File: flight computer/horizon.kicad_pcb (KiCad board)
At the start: 4 copper layers, 50.8 x 95.7 mm, 138 parts, among them J1 Micro_SD_Card_Det1, J10 Conn_01x02_Pin, J11 USB_C_Receptacle_USB2.0_16P, J12 Conn_01x04, J13 1x3 servo, J14 1x3 servo, J15 arming terminal, J16 arming terminal, J17 H9161TR-ND, J18 Conn_02x03_Counter_Clockwise, J19 Screw_Terminal_01x02, J20 Screw_Terminal_01x02, J21 Conn_02x03_Counter_Clockwise, J3 H9161TR-ND, J4 H9161TR-ND, J5 Screw_Term, J6 1x3 servo, J9 1x3 servo, Q2 DMG2301L, Q7 BSS138, Q8 IRLML6402, Q9 IRLML6402, SW1 CK_KMS2xxG, U1 MMCU, U13 LTC4412xS6, U15 AP2112K-3.3, U16 SX1262IMLTRT, U17 PE4259, U2 MKL02Z32VFG4, U3 TPS61200DRC, U6 GPS, U8 NAND, U9 TPS82130, Y1 Crystal, Y2 32MHz

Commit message: wiring we can finish in lit 1-2 days max
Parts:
- removed R14: 1.5k, Resistor_SMD:R_0603_1608Metric
- moved C46 162.5 mm to (215.5, 106.4), turned to -90 degrees
- moved J4 161.2 mm to (211.7, 100.8), turned to 180 degrees
- moved C49 160.2 mm to (213.2, 103.9), turned to 90 degrees
- moved R8 158.8 mm to (215.5, 103.3), turned to -90 degrees
- moved FL1 158.8 mm to (213.0, 110.0), turned to 90 degrees
- moved C48 154.3 mm to (210.6, 109.7), turned to 90 degrees
- moved U17 153.3 mm to (213.3, 107.0), turned to 90 degrees
- moved L10 152.7 mm to (211.3, 112.0)
- moved C47 151.9 mm to (209.0, 109.7), turned to 90 degrees
- moved C14 92.7 mm to (118.9, 142.7), turned to 45 degrees
- moved C37 90.0 mm to (124.9, 148.7)
- moved C40 89.9 mm to (123.5, 152.1)
- moved C38 89.6 mm to (121.5, 142.3), turned to 90 degrees
- moved C39 85.3 mm to (118.3, 148.5), turned to -45 degrees
- moved U16 84.6 mm to (124.9, 145.3)
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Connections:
- SAMD21G18A-AU1 pad 33: D+ DMCU-1 -> D- DMCU-1
- SAMD21G18A-AU1 pad 34: D- DMCU-1 -> D+ DMCU-1
- SAMD21G18A-AU2 pad 33: D+ DMCU-2 -> D- DMCU-1
- SAMD21G18A-AU2 pad 34: D- DMCU-2 -> D+ DMCU-1
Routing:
- net Earth: track 0.00 -> 14.4 mm
- net SX_XTB: track 0.00 -> 7.24 mm
- net SX_XTA: track 0.00 -> 6.27 mm
- net Net-(U16-VREG): track 0.00 -> 5.16 mm
- net +3V3: track 0.00 -> 5.07 mm
- net Net-(U16-DCC_SW): track 0.00 -> 3.23 mm

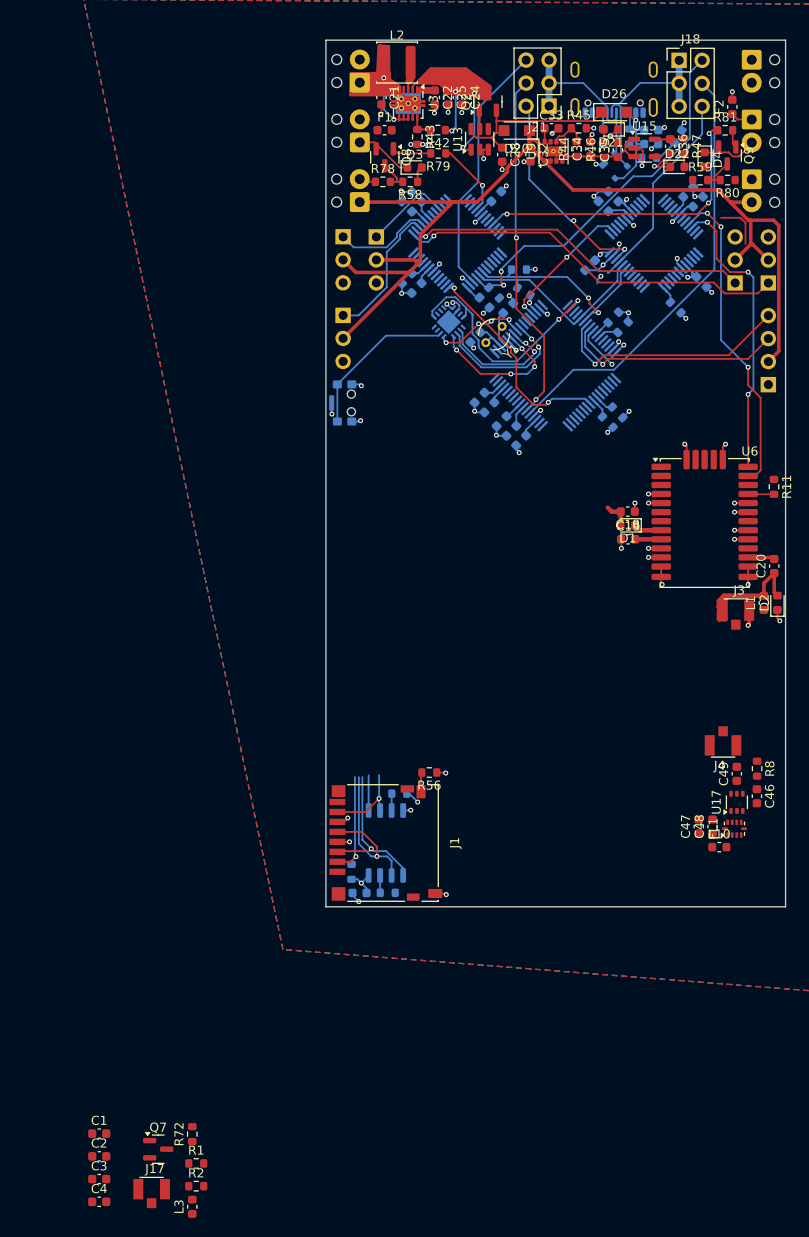
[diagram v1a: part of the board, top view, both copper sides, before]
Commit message: added BGM220SC12WGA2R
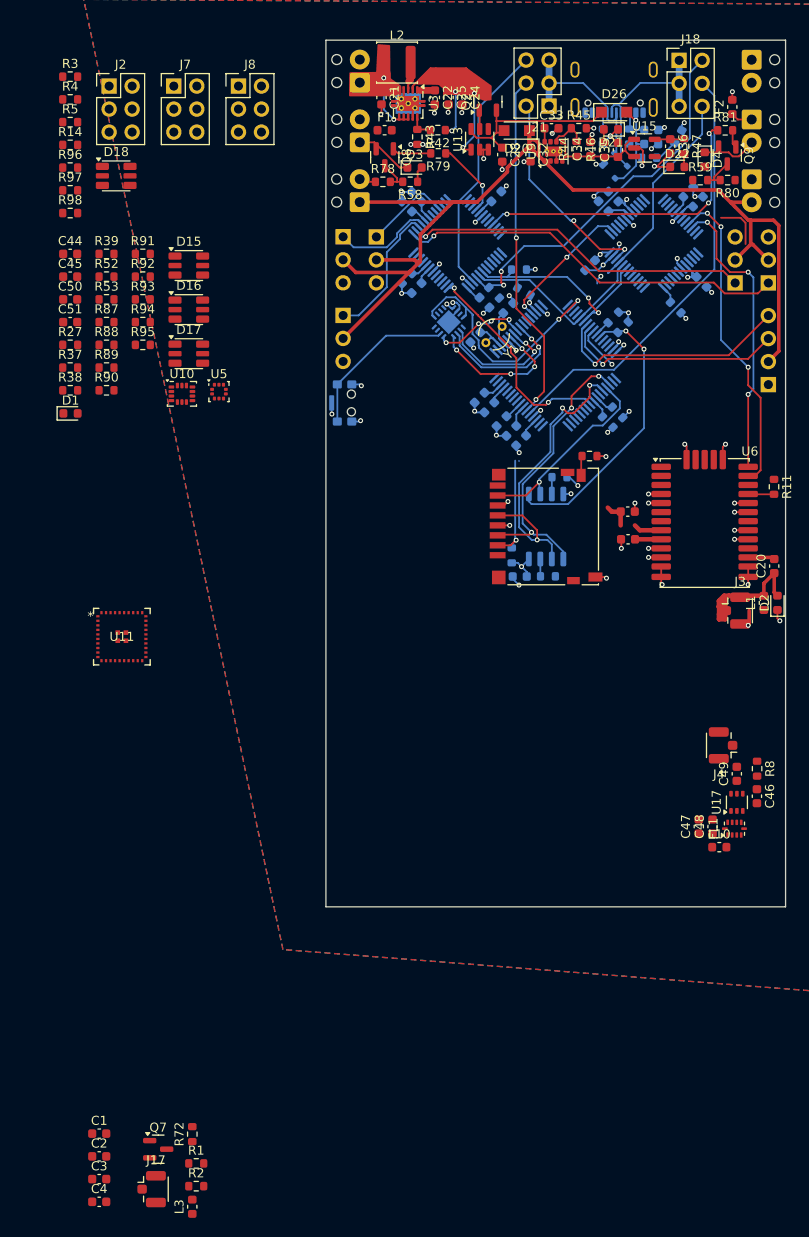
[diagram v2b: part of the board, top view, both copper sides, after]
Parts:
- added C44: 100nF, Capacitor_SMD:C_0603_1608Metric, F.Cu at (139.6, 46.5)
- added C45: 100nF, Capacitor_SMD:C_0603_1608Metric, F.Cu at (139.6, 49.0)
- added C50: 100nF, Capacitor_SMD:C_0603_1608Metric, F.Cu at (139.6, 51.5)
- added C51: 100nF, Capacitor_SMD:C_0603_1608Metric, F.Cu at (139.6, 54.0)
- added D15: SMLVN6RGB, LED_SMD:LED_ROHM_SMLVN6, F.Cu at (152.7, 47.8)
- added D16: SMLVN6RGB, LED_SMD:LED_ROHM_SMLVN6, F.Cu at (152.7, 52.6)
- added D17: SMLVN6RGB, LED_SMD:LED_ROHM_SMLVN6, F.Cu at (152.7, 57.5)
- added D18: SMLVN6RGB, LED_SMD:LED_ROHM_SMLVN6, F.Cu at (144.7, 37.9)
- added J2: Conn_02x03_Counter_Clockwise, Connector_PinHeader_2.54mm:PinHeader_2x03_P2.54mm_Vertical, F.Cu at (143.9, 28.0)
- added J7: Conn_02x03_Counter_Clockwise, Connector_PinHeader_2.54mm:PinHeader_2x03_P2.54mm_Vertical, F.Cu at (151.1, 28.0)
- added J8: Conn_02x03_Counter_Clockwise, Connector_PinHeader_2.54mm:PinHeader_2x03_P2.54mm_Vertical, F.Cu at (158.2, 28.0)
- added R14: 1.5k, Resistor_SMD:R_0603_1608Metric, F.Cu at (139.6, 34.5)
- added R27: 10k, Resistor_SMD:R_0603_1608Metric, F.Cu at (139.6, 56.5)
- added R3: 10k, Resistor_SMD:R_0603_1608Metric, F.Cu at (139.6, 26.9)
- added R37: 10k, Resistor_SMD:R_0603_1608Metric, F.Cu at (139.6, 59.0)
- added R38: 10k, Resistor_SMD:R_0603_1608Metric, F.Cu at (139.6, 61.5)
- added R39: 10k, Resistor_SMD:R_0603_1608Metric, F.Cu at (143.7, 46.5)
- added R4: 10k, Resistor_SMD:R_0603_1608Metric, F.Cu at (139.6, 29.4)
- added R5: 10k, Resistor_SMD:R_0603_1608Metric, F.Cu at (139.6, 31.9)
- added R52: 10k, Resistor_SMD:R_0603_1608Metric, F.Cu at (143.7, 49.0)
- added R53: 10k, Resistor_SMD:R_0603_1608Metric, F.Cu at (143.7, 51.5)
- added R87: 220, Resistor_SMD:R_0603_1608Metric, F.Cu at (143.7, 54.0)
- added R88: 220, Resistor_SMD:R_0603_1608Metric, F.Cu at (143.7, 56.5)
- added R89: 220, Resistor_SMD:R_0603_1608Metric, F.Cu at (143.7, 59.0)
- added R90: 220, Resistor_SMD:R_0603_1608Metric, F.Cu at (143.7, 61.5)
- added R91: 220, Resistor_SMD:R_0603_1608Metric, F.Cu at (147.7, 46.5)
- added R92: 220, Resistor_SMD:R_0603_1608Metric, F.Cu at (147.7, 49.0)
- added R93: 220, Resistor_SMD:R_0603_1608Metric, F.Cu at (147.7, 51.5)
- added R94: 220, Resistor_SMD:R_0603_1608Metric, F.Cu at (147.7, 54.0)
- added R95: 220, Resistor_SMD:R_0603_1608Metric, F.Cu at (147.7, 56.5)
- added R96: 220, Resistor_SMD:R_0603_1608Metric, F.Cu at (139.6, 37.0)
- added R97: 220, Resistor_SMD:R_0603_1608Metric, F.Cu at (139.6, 39.5)
- added R98: 220, Resistor_SMD:R_0603_1608Metric, F.Cu at (139.6, 42.0)
- added U10: LSM6DS3, Package_LGA:LGA-14_3x2.5mm_P0.5mm_LayoutBorder3x4y, F.Cu at (152.0, 61.9)
- added U11: BGM220SC12WGA2R, BGM220SC12WGA2R:BGM220S_SIL, F.Cu at (145.3, 88.7)
- added U5: LPS22HB, Package_LGA:ST_HLGA-10_2x2mm_P0.5mm_LayoutBorder3x2y, F.Cu at (156.1, 61.7)
- J17, J3, J4: footprint U.FL-R-SMT_01_:HRS_U.FL-R-SMT_01_ -> Connector_Coaxial:U.FL_Hirose_U.FL-R-SMT-1_Vertical
- moved D1 62.8 mm to (139.7, 64.1), turned to 0 degrees
- moved R55 39.2 mm to (188.4, 79.8)
- moved C15 39.2 mm to (189.3, 82.1)
- moved J1 39.2 mm to (192.2, 76.6)
- moved R12 39.2 mm to (193.7, 71.1)
- moved R54 39.2 mm to (192.4, 82.1)
- moved R56 39.2 mm to (197.0, 68.8)
- moved U8 39.2 mm to (192.2, 76.6)
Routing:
- net CS_NAND MMCU: track 6.13 -> 31.9 mm, vias 0 -> 2
- net SPI0_SCK MMCU: track 19.5 -> 34.3 mm, vias 1 -> 3
- net NAND_MOSI MMCU: track 17.4 -> 32.2 mm, vias 1 -> 3
- net NAND_MISO MMCU: track 9.17 -> 21.9 mm

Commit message: force push :'/
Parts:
- removed D15, D16, D17, D18: SMLVN6RGB, LED_SMD:LED_ROHM_SMLVN6
- removed J2, J7, J8: Conn_02x03_Counter_Clockwise, Connector_PinHeader_2.54mm:PinHeader_2x03_P2.54mm_Vertical
- removed R3, R4, R5: 10k, Resistor_SMD:R_0603_1608Metric
- removed R87, R88, R89, R90, R91, R92, R93, R94, R95, R96, R97, R98: 220, Resistor_SMD:R_0603_1608Metric
- moved C2 86.7 mm to (179.7, 67.6)
- moved C3 86.6 mm to (184.0, 72.5), turned to 180 degrees
- moved C1 85.8 mm to (182.7, 67.6), turned to 180 degrees
- moved R2 82.6 mm to (175.1, 69.6), turned to 90 degrees
- moved C4 80.1 mm to (177.2, 78.8), turned to 180 degrees
- moved L3 78.7 mm to (176.5, 76.6), turned to -90 degrees
- moved R1 77.3 mm to (175.1, 72.6), turned to -90 degrees
- moved C37 77.0 mm to (180.3, 95.3)
- moved C38 77.0 mm to (176.9, 88.8)
- moved C39 77.0 mm to (173.7, 95.1)
- moved C40 77.0 mm to (178.9, 98.6)
- moved U16 77.0 mm to (180.3, 91.9)
- moved C14 77.0 mm to (174.3, 89.3)
- moved L11 77.0 mm to (179.2, 97.0)
- moved Y2 77.0 mm to (174.9, 92.2)
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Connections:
- J18 pad 4: D+ MMCU -> D+ DMCU-2
- J18 pad 6: D+ DMCU-2 -> D+ MMCU
- R14 pad 1: D+ DMCU-1 -> D+ DMCU-2
- SAMD21G18A-AU2 pad 33: D- DMCU-1 -> D- DMCU-2
- SAMD21G18A-AU2 pad 34: D+ DMCU-1 -> D+ DMCU-2
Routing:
- net RS_GPS TMCU: track 0.00 -> 62.9 mm, vias 0 -> 3
- net CS_NAND MMCU: track 31.9 -> 4.32 mm, vias 2 -> 0
- net D+ DMCU-2: track 22.7 -> 0.00 mm
- net SPI0_SCK MMCU: track 34.3 -> 14.5 mm, vias 3 -> 1
- net NAND_MOSI MMCU: track 32.2 -> 15.2 mm, vias 3 -> 1
- net NAND_MISO MMCU: track 21.9 -> 8.61 mm
- net Earth: track 14.4 -> 24.8 mm
- net (no net): track 7.68 -> 0.00 mm
- net Net-(D2-A): track 20.4 -> 14.2 mm
- net Net-(D4-K): track 6.08 -> 0.00 mm
- net D+: track 21.4 -> 15.7 mm
- net D-: track 20.3 -> 15.2 mm
- net StatusLED_3: track 5.03 -> 0.00 mm, vias 1 -> 0
- net D+ MMCU: track 48.1 -> 43.5 mm, vias 0 -> 2
- net Net-(U17-CTRL): track 0.00 -> 3.75 mm
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
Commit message: fixes
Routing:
- net GND: track 94.6 -> 101.1 mm, vias 67 -> 71
- net +3.3V: track 59.9 -> 63.2 mm
- net Net-(J17-In): track 0.00 -> 3.25 mm
- net nRESET MMCU: track 27.4 -> 25.2 mm, vias 2 -> 0
- net Net-(U11-ANT_OUT): track 0.00 -> 1.81 mm
- net I2C0_SCL: track 22.3 -> 24.1 mm

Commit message: more stuff
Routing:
- net GND: track 101.1 -> 109.3 mm, vias 71 -> 75
- net D+ MMCU: track 43.5 -> 35.9 mm
- net Net-(J19-Pin_2): track 0.00 -> 2.45 mm
- net Net-(D4-A): track 0.00 -> 2.04 mm
- net Net-(J16-Pin_1): track 0.00 -> 1.87 mm
- net Net-(D4-K): track 0.00 -> 1.78 mm
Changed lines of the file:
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@@
 			(at 0 -1.43 0)
 			(layer "F.SilkS")
+			(hide yes)
 			(effects
 				(font
@@
 			(at 0 -1.43 0)
 			(layer "F.SilkS")
+			(hide yes)
 			(effects
 				(font
@@
 			(at 0 -1.43 90)
 			(layer "F.SilkS")
+			(hide yes)
 			(effects
 				(font
@@
 			(at 0 -2.4 90)
 			(layer "F.SilkS")
+			(hide yes)
 			(effects
 				(font
@@
 			(at 0 -1.43 0)
 			(layer "F.SilkS")
+			(hide yes)
 			(effects
 				(font
@@
 			(at 0 -1.43 90)
 			(layer "F.SilkS")
+			(hide yes)
 			(effects
 				(font
@@
 			(at 0 -1.43 0)
 			(layer "F.SilkS")
+			(hide yes)
 			(effects
 				(font
@@
 			(at 0 -1.43 90)
 			(layer "F.SilkS")
+			(hide yes)
 			(effects
 				(font
@@
 			(at 0 1.43 0)
 			(layer "B.SilkS")
+			(hide yes)
 			(effects
 				(font
@@
 			(at -0.000001 1.43 60)
 			(layer "B.SilkS")
+			(hide yes)
 			(effects
 				(font
@@
 			(at 0 1.43 45)
 			(layer "B.SilkS")
+			(hide yes)
 			(effects
 				(font
@@
 	)
 	(via
+		(at 195 29)
+		(size 0.55)
+		(drill 0.3)
+		(layers "F.Cu" "B.Cu")
+		(net 1)
+	)
+	(via
 		(at 199.28 33.48)
 		(size 0.55)
@@
 	)
 	(via
+		(at 205 29.5)
+		(size 0.55)
+		(drill 0.3)
+		(layers "F.Cu" "B.Cu")
+		(net 1)
+	)
+	(via
 		(at 205 83)
 		(size 0.55)
@@
 	)
 	(via
+		(at 204.5 25)
+		(size 0.55)
+		(drill 0.3)
+		(layers "F.Cu" "B.Cu")
+		(net 1)
+	)
+	(via
 		(at 197.46 32.6)
 		(size 0.55)
@@
 	)
 	(via
+		(at 196 25)
+		(size 0.55)
+		(drill 0.3)
+		(layers "F.Cu" "B.Cu")
+		(net 1)
+	)
+	(via
 		(at 182.94 49.15)
 		(size 0.55)
@@
 	)
 	(segment
+		(start 195.38 30.32)
+		(end 195.925 30.32)
+		(width 0.2)
+		(layer "B.Cu")
+		(net 1)
+	)
+	(segment
 		(start 188.12 51.1)
 		(end 188.558008 51.538008)
@@
 	)
 	(segment
+		(start 195.38 25.62)
+		(end 196 25)
+		(width 0.2)
+		(layer "B.Cu")
+		(net 1)
+	)
+	(segment
 		(start 186.766016 66.576016)
 		(end 186.7 66.51)
@@
 	)
 	(segment
+		(start 195.38 26.14)
+		(end 195.38 25.62)
+		(width 0.2)
+		(layer "B.Cu")
+		(net 1)
+	)
+	(segment
 		(start 184.193078 56.873079)
 		(end 183.833984 56.513984)
@@
 	)
 	(segment
+		(start 204.02 26.14)
+		(end 204.02 25.48)
+		(width 0.2)
+		(layer "B.Cu")
+		(net 1)
+	)
+	(segment
 		(start 176.273984 49.736016)
 		(end 176.273984 50.816016)
@@
 	)
 	(segment
+		(start 203.475 30.32)
+		(end 202.9 30.895)
+		(width 0.2)
+		(layer "B.Cu")
+		(net 1)
+	)
+	(segment
 		(start 192.019258 53.041367)
 		(end 192.247351 53.041367)
@@
 	)
 	(segment
+		(start 195.925 30.32)
+		(end 196.5 30.895)
+		(width 0.2)
+		(layer "B.Cu")
+		(net 1)
+	)
+	(segment
 		(start 201.766446 43.35)
 		(end 201.86 43.35)
@@
 	)
 	(segment
+		(start 204.02 30.32)
+		(end 203.475 30.32)
+		(width 0.2)
+		(layer "B.Cu")
+		(net 1)
+	)
+	(segment
 		(start 206.67 47.546446)
 		(end 206.67 46.99)
@@
 	)
 	(segment
+		(start 204.02 30.32)
+		(end 204.18 30.32)
+		(width 0.2)
+		(layer "B.Cu")
+		(net 1)
+	)
+	(segment
 		(start 168.515 64.145)
 		(end 168.54 64.17)
@@
 	)
 	(segment
+		(start 204.02 25.48)
+		(end 204.5 25)
+		(width 0.2)
+		(layer "B.Cu")
+		(net 1)
+	)
+	(segment
 		(start 204.57 34.36)
 		(end 204.34 34.36)
@@
 	)
 	(segment
+		(start 195.38 29.38)
+		(end 195 29)
+		(width 0.2)
+		(layer "B.Cu")
+		(net 1)
+	)
+	(segment
 		(start 200.2 56.417891)
 		(end 200.2 56.18)
@@
 	)
 	(segment
+		(start 195.38 30.32)
+		(end 195.38 29.38)
+		(width 0.2)
+		(layer "B.Cu")
+		(net 1)
+	)
+	(segment
 		(start 182.372722 52.831973)
 		(end 181.48 53.724695)
@@
 	)
 	(segment
+		(start 204.18 30.32)
+		(end 205 29.5)
+		(width 0.2)
+		(layer "B.Cu")
+		(net 1)
+	)
+	(segment
 		(start 170.74 60.895)
 		(end 171.635 60.895)
@@
 	)
 	(segment
+		(start 208.413372 48.582712)
+		(end 208.413372 48.892105)
+		(width 0.2)
+		(layer "B.Cu")
+		(net 2)
+	)
+	(segment
+		(start 208.30033 48.46967)
+		(end 208.413372 48.582712)
+		(width 0.2)
+		(layer "B.Cu")
+		(net 2)
+	)
+	(segment
 		(start 200.89033 40.66967)
 		(end 200.89033 41.05967)
@@
 	)
 	(segment
+		(start 209.7 35.275)
+		(end 210.65 35.275)
+		(width 0.2)
+		(layer "F.Cu")
+		(net 11)
+	)
+	(segment
+		(start 210.65 35.275)
+		(end 211.24 34.685)
+		(width 0.2)
+		(layer "F.Cu")
+		(net 11)
+	)
+	(segment
+		(start 172.82 32.83)
+		(end 173.575 32.83)
+		(width 0.2)
+		(layer "F.Cu")
+		(net 13)
+	)
+	(segment
+		(start 171.62 31.63)
+		(end 172.82 32.83)
+		(width 0.2)
+		(layer "F.Cu")
+		(net 13)
+	)
+	(segment
 		(start 177.325979 43.088697)
 		(end 176.058 44.356676)
@@
 	)
 	(segment
-		(start 184.774078 56.63242)
-		(end 184.774078 56.834078)
+		(start 184.063716 55.403672)
+		(end 184.739 56.078956)
 		(width 0.2)
 		(layer "B.Cu")
@@
 	)
 	(segment
-		(start 184.739 56.011076)
-		(end 184.739 56.597342)
+		(start 182.953794 52.046206)
+		(end 184.063716 53.156128)
 		(width 0.2)
 		(layer "B.Cu")
@@
 	(segment
 		(start 182.186589 51.279)
-		(end 183.329649 52.42206)
+		(end 182.953794 52.046206)
 		(width 0.2)
 		(layer "B.Cu")
@@
 	)
 	(segment
-		(start 184.739 56.597342)
-		(end 184.774078 56.63242)
+		(start 184.739 56.621786)
+		(end 186.474893 58.357679)
 		(width 0.2)
 		(layer "B.Cu")
@@
 	)
 	(segment
-		(start 184.774078 56.834078)
-		(end 186.297679 58.357679)
+		(start 184.739 56.078956)
+		(end 184.739 56.621786)
 		(width 0.2)
 		(layer "B.Cu")
@@
 	)
 	(segment
-		(start 186.297679 58.357679)
+		(start 187 58.357679)
 		(end 188.952321 58.357679)
 		(width 0.2)
@@
 	)
 	(segment
-		(start 184.063716 55.335792)
-		(end 184.739 56.011076)
-		(width 0.2)
-		(layer "B.Cu")
-		(net 22)
-	)
-	(segment
 		(start 188.952321 58.357679)
 		(end 191.155 56.155)
@@
 	)
 	(segment
-		(start 184.063716 53.268695)
-		(end 184.063716 55.335792)
+		(start 184.063716 53.156128)
+		(end 184.063716 55.403672)
 		(width 0.2)
 		(layer "B.Cu")
@@
 	)
 	(segment
-		(start 183.329649 52.42206)
-		(end 184.12 53.212411)
+		(start 179.630351 53.28926)
+		(end 179.630351 52.805398)
 		(width 0.2)
 		(layer "B.Cu")
@@
 	)
 	(segment
-		(start 179.630351 53.28926)
-		(end 179.630351 52.805398)
+		(start 186.474893 58.357679)
+		(end 187 58.357679)
 		(width 0.2)
 		(layer "B.Cu")
@@
 	)
 	(segment
-		(start 184.12 53.212411)
-		(end 184.063716 53.268695)
+		(start 182.953794 52.046206)
+		(end 183.329649 52.42206)
 		(width 0.2)
 		(layer "B.Cu")
@@
 	)
 	(segment
-		(start 209.42 33.3)
-		(end 204.01 38.71)
-		(width 0.2)
-		(layer "B.Cu")
-		(net 27)
-	)
-	(segment
 		(start 191.491449 63.008551)
 		(end 191.49 63.008551)
@@
 	)
 	(segment
+		(start 213.15 38.25)
+		(end 213.06 38.34)
+		(width 0.2)
+		(layer "F.Cu")
+		(net 154)
+	)
+	(segment
+		(start 214.8925 38.25)
+		(end 213.15 38.25)
+		(width 0.2)
+		(layer "F.Cu")
+		(net 154)
+	)
+	(segment
 		(start 176.96406 31.639289)
 		(end 175.96406 31.639289)
@@
 	)
 	(segment
+		(start 209.7 37.02)
+		(end 208.38 38.34)
+		(width 0.2)
+		(layer "F.Cu")
+		(net 161)
+	)
+	(segment
+		(start 209.7 36.85)
+		(end 209.7 37.02)
+		(width 0.2)
+		(layer "F.Cu")
+		(net 161)
+	)
+	(segment

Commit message: more bl routing
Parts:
- moved R14 7.88 mm to (201.7, 51.3), turned to -45 degrees
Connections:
- net SD_DETECT renamed Net-(J1-DET)
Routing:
- net D+ DMCU-2: track 0.00 -> 39.6 mm, vias 0 -> 2
- net I2C0_SCL: track 24.1 -> 53.4 mm, vias 0 -> 1
- net SWCLK DMCU-1: track 0.00 -> 27.4 mm, vias 0 -> 1
- net I2C0_SDA: track 25.7 -> 52.8 mm, vias 2 -> 3
- net BGM_INT: track 0.00 -> 23.0 mm, vias 0 -> 1
- net GND: track 109.3 -> 119.2 mm, vias 75 -> 78
- net D+ MMCU: track 35.9 -> 44.4 mm
- net +3.3V: track 63.7 -> 71.8 mm
- net Net-(U11-DECOUPLE): track 0.00 -> 1.44 mm
